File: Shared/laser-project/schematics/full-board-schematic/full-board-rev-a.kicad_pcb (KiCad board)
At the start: 2 copper layers, 112 x 60 mm, 44 parts, among them CON1 USB-MINI-B, CON2 JTAG-10MIL-HDR, SW1 PUSHSWITCH, SW2 PUSHSWITCH, T1 OP598C, T2 BSS138, T3 BSS138, U1 AT90USB1286, U2 DS1077, U3 AD8302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

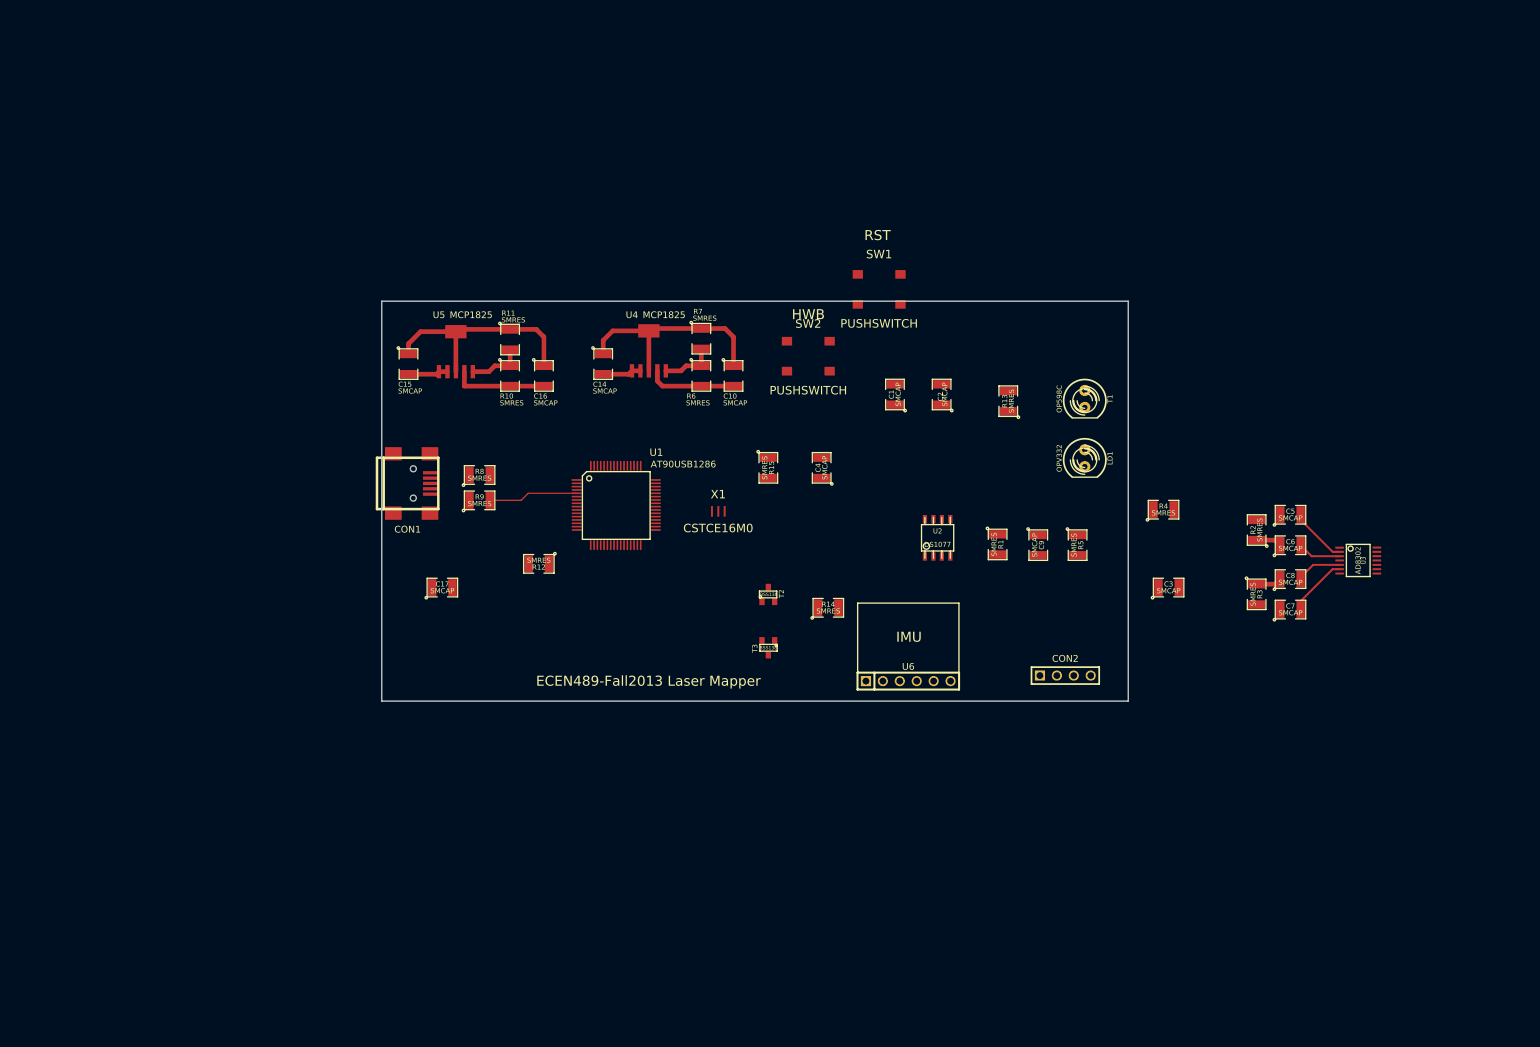
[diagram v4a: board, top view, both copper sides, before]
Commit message: More routing progress.
Also mounted a teensy++2.0 to the board.
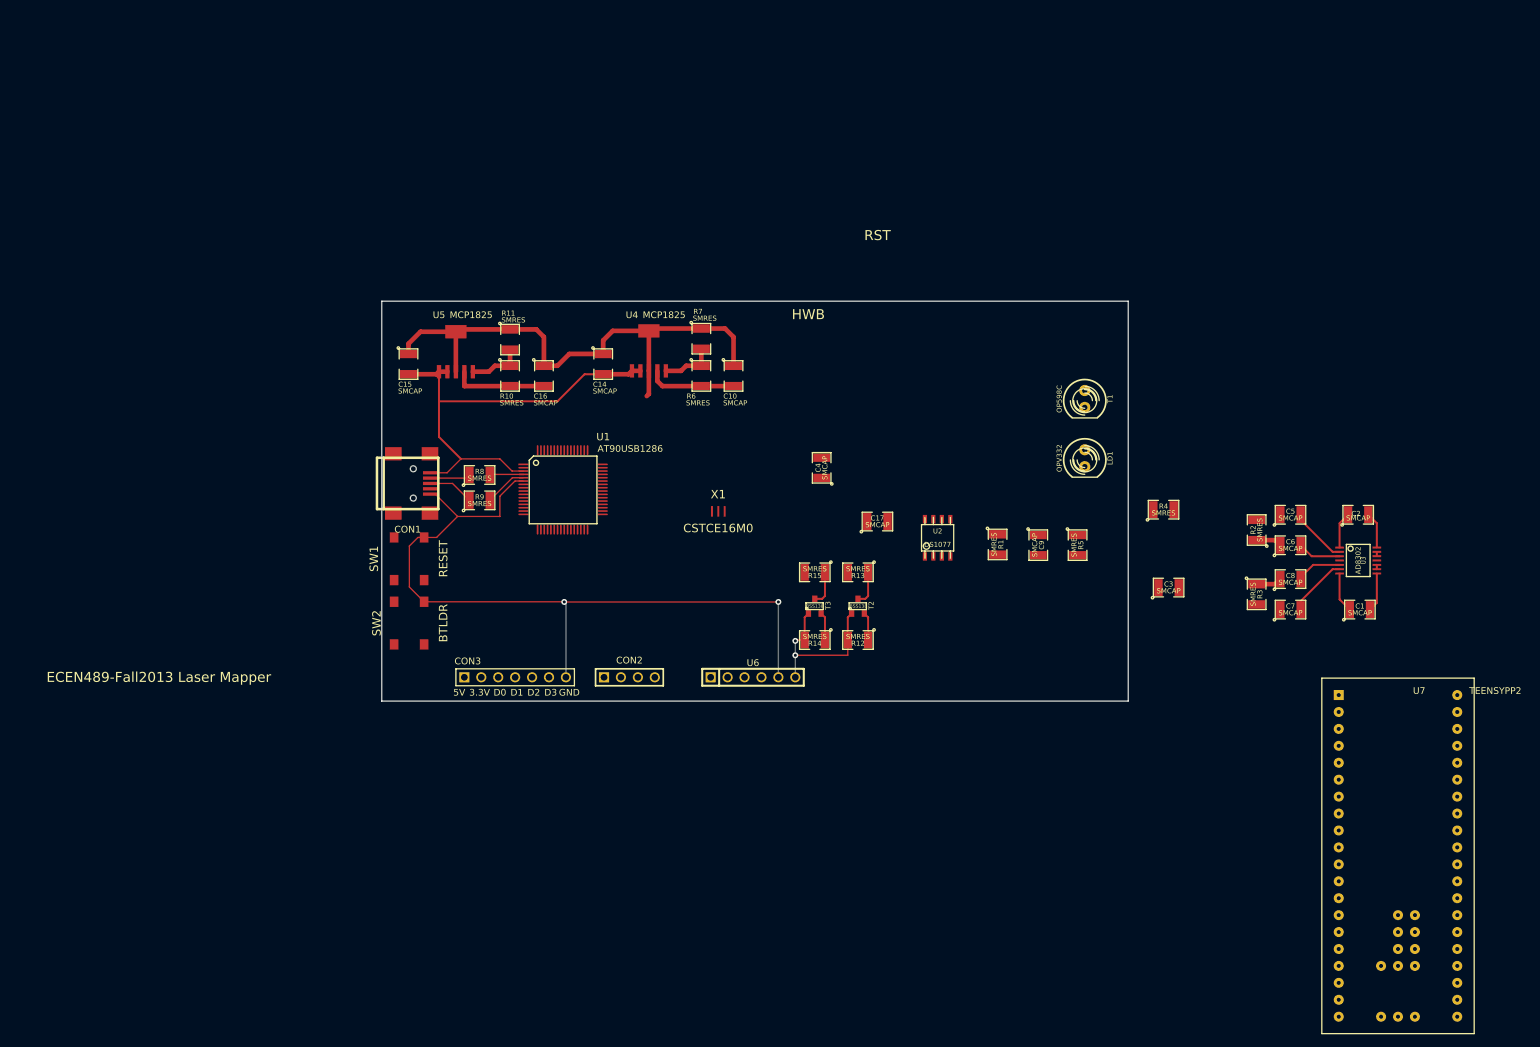
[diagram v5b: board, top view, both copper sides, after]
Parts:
- added CON3: ENCODER-10MIL-HEADER, encoder-10mil-header, F.Cu at (108.2, 122.4)
- added U7: TEENSYPP2, Teensy++2.0, F.Cu at (245.1, 148.6)
- SW1: value PUSHSWITCH -> RESET
- SW2: value PUSHSWITCH -> BTLDR
- moved SW1 84.4 mm to (93.9, 104.6), turned to 270 degrees
- moved C1 76.9 mm to (238.8, 112.3), turned to 0 degrees
- moved SW2 75.2 mm to (93.9, 114.3), turned to 270 degrees
- moved C17 66.0 mm to (166.4, 99.1)
- moved CON2 65.4 mm to (129.2, 122.4)
- moved C2 65.1 mm to (238.5, 98.0), turned to 0 degrees
- moved R12 49.2 mm to (163.4, 116.8)
- moved R13 34.2 mm to (163.4, 106.7), turned to 180 degrees
- moved U6 23.3 mm to (147.7, 122.4)
- moved R15 17.2 mm to (157.0, 106.7), turned to 180 degrees
- moved T2 13.6 mm to (163.4, 111.8)
- moved T3 9.36 mm to (157.0, 111.8), turned to 0 degrees
- moved U1 8.31 mm to (119.1, 94.2)
- moved R14 5.25 mm to (157.0, 116.8), turned to 180 degrees
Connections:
- CON1 pad 2: /usb_d- -> N-000002
- CON1 pad 3: /usb_d+ -> N-000001
- CON2 pad 3: /jtag_tdi -> /jtag_tdo
- CON2 pad 4: /jtag_tdo -> /jtag_tdi
- R8 pad 1: /usb_d- -> N-000002
- R8 pad 2: N-000005 -> /usb_d-
- R9 pad 1: /usb_d+ -> N-000001
- R9 pad 2: N-000004 -> /usb_d+
- T2 pad 2: /twi_scl_5V -> /twi_scl_3.3V
- T2 pad 3: /twi_scl_3.3V -> /twi_scl_5V
- T3 pad 2: /twi_sda_5V -> /twi_sda_3.3V
- T3 pad 3: /twi_sda_3.3V -> /twi_sda_5V
- U1 pad 1: (no net) -> /encoder-interface-2
- U1 pad 18: (no net) -> /encoder-interface-0
- U1 pad 19: (no net) -> /encoder-interface-1
- U1 pad 2: (no net) -> /encoder-interface-3
- U1 pad 4: N-000005 -> /usb_d-
- U1 pad 5: N-000004 -> /usb_d+
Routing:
- net GND: track 74.4 -> 213.0 mm, vias 0 -> 2
- net /usb_5V: track 11.8 -> 68.1 mm
- net /regulator_3.3V: track 14.1 -> 39.6 mm, vias 0 -> 2
- net N-000004: track 13.5 -> 0.00 mm
- net N-000001: track 0.00 -> 6.87 mm
- net /usb_d+: track 0.00 -> 6.46 mm
- net N-000002: track 0.00 -> 6.02 mm
- net N-0000042: track 0.00 -> 5.83 mm
- net N-0000043: track 0.00 -> 5.44 mm
- net /twi_sda_5V: track 0.00 -> 5.26 mm
- net /twi_scl_5V: track 0.00 -> 5.26 mm
- net /usb_d-: track 0.00 -> 5.09 mm
- net /twi_sda_3.3V: track 0.00 -> 4.22 mm
- net /twi_scl_3.3V: track 0.00 -> 4.22 mm
- net /ad8302_phs: track 0.00 -> 0.65 mm
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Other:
- board text removed: "IMU"

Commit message: Routing almost complete.
It gives me a headache.
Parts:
- moved U7 76.8 mm to (177.0, 113.0), turned to 90 degrees
- moved C17 61.0 mm to (105.4, 101.3)
- moved C2 57.5 mm to (188.8, 69.1)
- moved C5 57.5 mm to (178.7, 69.1)
- moved C6 57.5 mm to (178.7, 73.7)
- moved C7 57.5 mm to (178.7, 83.3)
- moved C8 57.5 mm to (178.7, 78.7)
- moved U3 57.5 mm to (188.8, 75.9)
- moved C1 57.5 mm to (189.1, 83.3)
- moved R2 57.5 mm to (173.6, 71.4)
- moved R3 57.5 mm to (173.6, 81.0)
- moved C3 51.6 mm to (162.9, 88.0), turned to 90 degrees
- moved R4 48.8 mm to (162.9, 81.9), turned to 90 degrees
- moved C9 42.1 mm to (164.8, 69.2), turned to 0 degrees
- moved U2 30.5 mm to (160.7, 74.8), turned to 90 degrees
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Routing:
- net /regulator_5V: track 13.3 -> 215.0 mm, vias 0 -> 9
- net GND: track 213.0 -> 407.6 mm, vias 2 -> 15
- net /twi_sda_5V: track 5.26 -> 104.9 mm, vias 0 -> 4
- net /twi_scl_5V: track 5.26 -> 96.3 mm, vias 0 -> 2
- net /mod_sig_1: track 0.00 -> 64.0 mm
- net /hwb_sig: track 0.00 -> 54.6 mm, vias 0 -> 2
- net /twi_scl_3.3V: track 4.22 -> 47.7 mm, vias 0 -> 2
- net /jtag_tck: track 0.00 -> 42.3 mm, vias 0 -> 2
- net /jtag_tdi: track 0.00 -> 42.3 mm, vias 0 -> 2
- net /jtag_tms: track 0.00 -> 42.2 mm, vias 0 -> 2
- net /jtag_tdo: track 0.00 -> 41.9 mm, vias 0 -> 2
- net /return_sig: track 0.00 -> 37.4 mm
- net /twi_sda_3.3V: track 4.22 -> 38.6 mm, vias 0 -> 2
- net /reset_sig: track 0.00 -> 30.0 mm, vias 0 -> 2
- net /ad8302_vpos: track 0.00 -> 29.3 mm, vias 0 -> 2
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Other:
- board text removed: "HWB"
- board text removed: "RST"
